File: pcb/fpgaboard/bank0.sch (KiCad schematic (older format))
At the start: 19 parts, among them J3 CONN_02X03, J4 CONN_01X02, J5 CONN_02X03, J6 CONN_01X21, J7 CONN_02X05, U3 iCE40-HX8K-CT256, U6 74LVCH8T245, X2 16.777216M

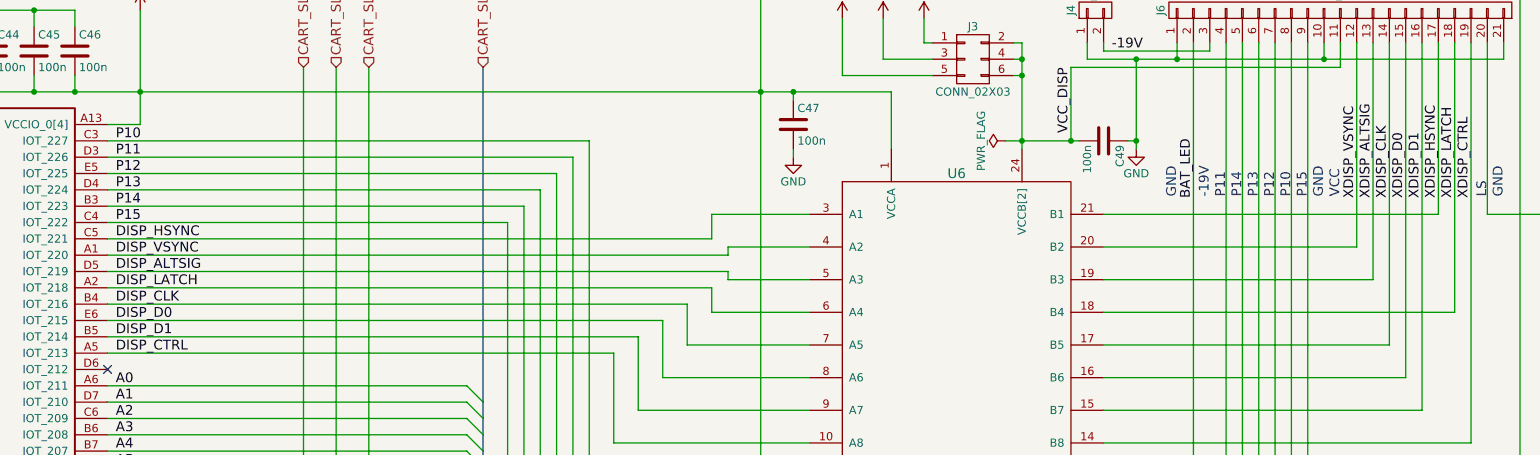
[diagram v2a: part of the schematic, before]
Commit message: fix labeling of D0&D1 LCD signals
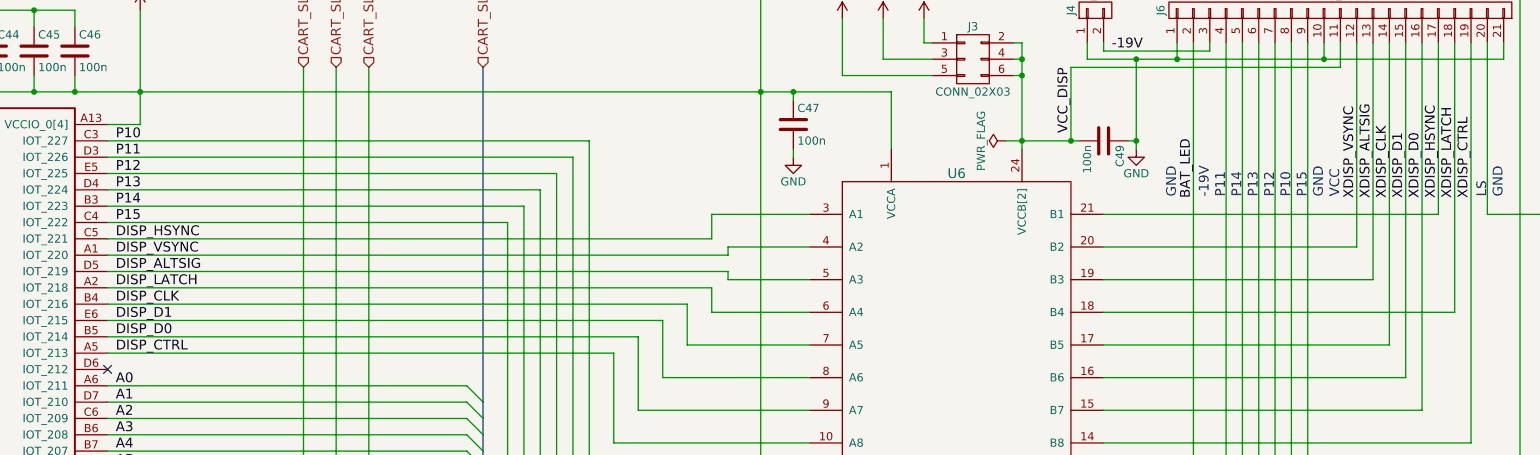
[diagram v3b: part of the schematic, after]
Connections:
- net DISP_D0: now also U3.B5 (IOT_214), U6.9 (A7); no longer U3.E6 (IOT_215), U6.8 (A6)
- net DISP_D1: now also U3.E6 (IOT_215), U6.8 (A6); no longer U3.B5 (IOT_214), U6.9 (A7)
- net XDISP_D0: now also J6.16 (P16), U6.15 (B7); no longer J6.15 (P15), U6.16 (B6)
- net XDISP_D1: now also J6.15 (P15), U6.16 (B6); no longer J6.16 (P16), U6.15 (B7)
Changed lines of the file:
@@
 Sheet 3 11
 Title "Game Boy reverse eng. FPGA board"
-Date "2019-08-17"
+Date "2019-10-06"
 Rev "1"
 Comp "Author: Michael Singer"
@@
 DISP_CLK
 Text Label 2150 2950 0    60   ~ 0
+DISP_D1
+Text Label 2150 3050 0    60   ~ 0
 DISP_D0
-Text Label 2150 3050 0    60   ~ 0
-DISP_D1
 Text Label 2150 3150 0    60   ~ 0
 DISP_CTRL
@@
 XDISP_CLK
 Text Label 10050 2200 1    60   ~ 0
+XDISP_D1
+Text Label 10150 2200 1    60   ~ 0
 XDISP_D0
-Text Label 10150 2200 1    60   ~ 0
-XDISP_D1
 Text Label 10250 2200 1    60   ~ 0
 XDISP_HSYNC

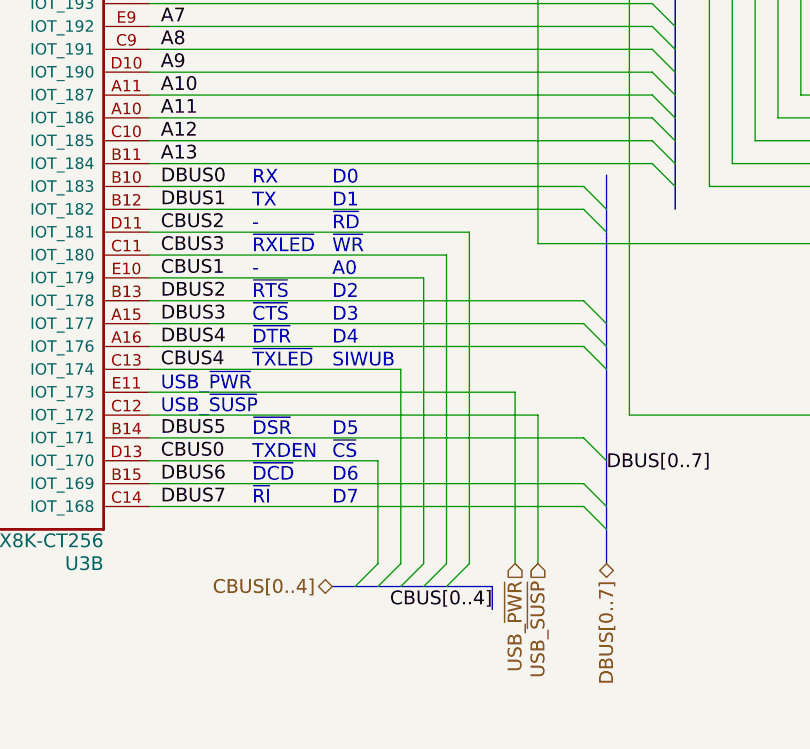
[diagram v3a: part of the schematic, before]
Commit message: added labels for FT245 configuration of FTDI
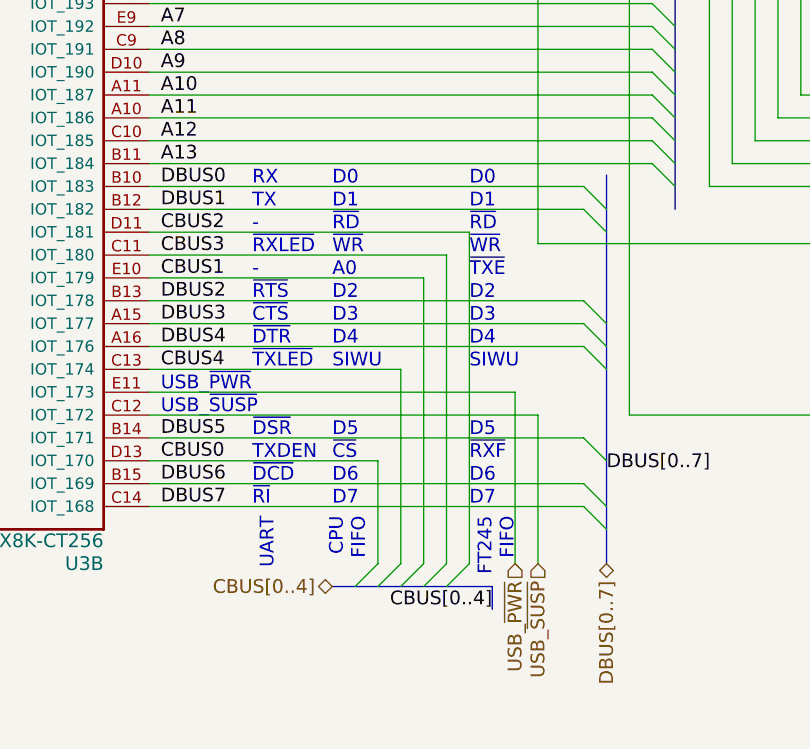
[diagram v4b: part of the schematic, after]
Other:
- note added: "CPU\nFIFO"
- note added: "FT245\nFIFO"
- note added: "SIWU"
- note added: "UART"
- note added: "~RXF"
- note added: "~TXE"
- note removed: "SIWUB"
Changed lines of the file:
@@
 Sheet 3 11
 Title "Game Boy reverse eng. FPGA board"
-Date "2019-10-06"
+Date "2019-10-26"
 Rev "1"
 Comp "Author: Michael Singer"
@@
 ~TXLED
 Text Notes 2900 6350 0    60   ~ 0
-SIWUB
+SIWU
 Text Notes 2150 6450 0    60   ~ 0
 USB_~PWR
@@
 Text Label 10450 2200 1    60   ~ 0
 XDISP_CTRL
+Text Notes 3500 5550 0    60   ~ 0
+D0
+Text Notes 3500 5650 0    60   ~ 0
+D1
+Text Notes 3500 5750 0    60   ~ 0
+~RD
+Text Notes 3500 5850 0    60   ~ 0
+~WR
+Text Notes 3500 5950 0    60   ~ 0
+~TXE
+Text Notes 3500 6050 0    60   ~ 0
+D2
+Text Notes 3500 6150 0    60   ~ 0
+D3
+Text Notes 3500 6250 0    60   ~ 0
+D4
+Text Notes 3500 6350 0    60   ~ 0
+SIWU
+Text Notes 3500 6650 0    60   ~ 0
+D5
+Text Notes 3500 6750 0    60   ~ 0
+~RXF
+Text Notes 3500 6850 0    60   ~ 0
+D6
+Text Notes 3500 6950 0    60   ~ 0
+D7
+Text Notes 2650 7000 3    60   ~ 0
+UART
+Text Notes 3050 7000 3    60   ~ 0
+CPU\nFIFO
+Text Notes 3700 7000 3    60   ~ 0
+FT245\nFIFO
 $EndSCHEMATC
